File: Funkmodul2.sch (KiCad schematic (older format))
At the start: 48 parts, among them Q1 SSM3J334RLFTR-ND, Q2 AO3414, U1 MC74HC4538A, U2 MAX892, U3 ATMEGA128-16AU, Y1 Crystal_GND24

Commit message: Adds new unit
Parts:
- removed C1, C4: 10µF, Capacitors_SMD:C_1210_HandSoldering, symbol C
- removed C10, C11, C12, C20, C5, C6: 100nF, Capacitors_SMD:C_0603_HandSoldering, symbol C
- removed C2: 1µF, Capacitors_SMD:C_1210_HandSoldering, symbol C
- removed C3: 1nF, Capacitors_SMD:C_0603_HandSoldering, symbol C
- removed C7, C8: 10pF, Capacitors_SMD:C_0603_HandSoldering, symbol C
- removed C9: 10nF, Capacitors_SMD:C_0603_HandSoldering, symbol C
- removed D1, D2, D3, D4, D5, D6, D7, D8, D9: TS4148C, Diodes_SMD:D_0603, symbol D
- removed D10: DZ2J036M0LCT-ND, Diodes_SMD:D_SOD-323F, symbol D_Zener
- removed L1: 10nH, Inductors_SMD:L_0603_HandSoldering, symbol Ferrite_Bead
- removed Q1: SSM3J334RLFTR-ND, TO_SOT_Packages_SMD:SOT-23, symbol Q_PMOS_DGS
- removed Q2: AO3414, TO_SOT_Packages_SMD:SOT-23, symbol Q_NMOS_DGS
- removed R1: 22k, Resistors_SMD:R_0603_HandSoldering, symbol R
- removed R10: 15k, Resistors_SMD:R_0603_HandSoldering, symbol R
- removed R11, R14, R15, R16, R17, R2, R3, R6, R7, R9: 100k, Resistors_SMD:R_0603_HandSoldering, symbol R
- removed R12, R13, R8: 10k, Resistors_SMD:R_0603_HandSoldering, symbol R
- removed R18, R5: 100R, Resistors_SMD:R_0603_HandSoldering, symbol R
- removed R4: 47R, Resistors_SMD:R_0603_HandSoldering, symbol R
- removed U1: MC74HC4538A, Housings_SOIC:SOIC-16_3.9x9.9mm_Pitch1.27mm, symbol MC74HC4538A
- removed U2: MAX892, Maxim:µMAX-8, symbol MAX892
- removed U3: ATMEGA128-16AU, Housings_QFP:TQFP-64_14x14mm_Pitch0.8mm, symbol ATMEGA128-16AU
- removed Y1: Crystal_GND24, Crystals:Crystal_SMD_3225-4pin_3.2x2.5mm_HandSoldering, symbol Crystal_GND24
- added C21, C25: 10µF, Capacitors_SMD:C_1210_HandSoldering, symbol C
- added C22, C26, C27, C31, C32, C33: 100nF, Capacitors_SMD:C_0603_HandSoldering, symbol C
- added C23: 1µF, Capacitors_SMD:C_1210_HandSoldering, symbol C
- added C24: 1nF, Capacitors_SMD:C_0603_HandSoldering, symbol C
- added C28, C29: 10pF, Capacitors_SMD:C_0603_HandSoldering, symbol C
- added C30: 10nF, Capacitors_SMD:C_0603_HandSoldering, symbol C
- added D19, D20, D21, D22, D23, D24, D25, D26, D27: TS4148C, Diodes_SMD:D_0603, symbol D
- added D28: DZ2J036M0LCT-ND, Diodes_SMD:D_SOD-323F, symbol D_Zener
- added L3: 10nH, Inductors_SMD:L_0603_HandSoldering, symbol Ferrite_Bead
- added Q10: AO3414, TO_SOT_Packages_SMD:SOT-23, symbol Q_NMOS_DGS
- added Q9: SSM3J334RLFTR-ND, TO_SOT_Packages_SMD:SOT-23, symbol Q_PMOS_DGS
- added R46: 22k, Resistors_SMD:R_0603_HandSoldering, symbol R
- added R47, R48, R51, R52, R54, R56, R59, R60, R61, R62: 100k, Resistors_SMD:R_0603_HandSoldering, symbol R
- added R49: 47R, Resistors_SMD:R_0603_HandSoldering, symbol R
- added R50, R63: 100R, Resistors_SMD:R_0603_HandSoldering, symbol R
- added R53, R57, R58: 10k, Resistors_SMD:R_0603_HandSoldering, symbol R
- added R55: 15k, Resistors_SMD:R_0603_HandSoldering, symbol R
- added U6: MC74HC4538A, Housings_SOIC:SOIC-16_3.9x9.9mm_Pitch1.27mm, symbol MC74HC4538A
- added U7: MAX892, Maxim:µMAX-8, symbol MAX892
- added U8: ATMEGA128-16AU, Housings_QFP:TQFP-64_14x14mm_Pitch0.8mm, symbol ATMEGA128-16AU
- added Y2: Crystal_GND24, Crystals:Crystal_SMD_3225-4pin_3.2x2.5mm_HandSoldering, symbol Crystal_GND24

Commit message: Places µC of second module
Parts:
- Q9: symbol Q_PMOS_DGS -> Q_PMOS_SGD
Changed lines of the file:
@@
 $EndComp
 $Comp
-L GND #PWR57
+L GND #PWR047
 U 1 1 59B7E482
 P 3200 1650
-F 0 "#PWR57" H 3200 1400 50  0001 C CNN
+F 0 "#PWR047" H 3200 1400 50  0001 C CNN
 F 1 "GND" H 3200 1500 50  0000 C CNN
 F 2 "" H 3200 1650 50  0001 C CNN
@@
 $EndComp
 $Comp
-L GND #PWR53
+L GND #PWR048
 U 1 1 59FF9D56
 P 2250 1350
-F 0 "#PWR53" H 2250 1100 50  0001 C CNN
+F 0 "#PWR048" H 2250 1100 50  0001 C CNN
 F 1 "GND" H 2250 1200 50  0000 C CNN
 F 2 "" H 2250 1350 50  0001 C CNN
@@
 VCC
 $Comp
-L GND #PWR59
+L GND #PWR049
 U 1 1 59FF9D57
 P 3750 2450
-F 0 "#PWR59" H 3750 2200 50  0001 C CNN
+F 0 "#PWR049" H 3750 2200 50  0001 C CNN
 F 1 "GND" H 3750 2300 50  0000 C CNN
 F 2 "" H 3750 2450 50  0001 C CNN
@@
 $EndComp
 $Comp
-L GND #PWR60
+L GND #PWR050
 U 1 1 59FF9D58
 P 3750 2850
-F 0 "#PWR60" H 3750 2600 50  0001 C CNN
+F 0 "#PWR050" H 3750 2600 50  0001 C CNN
 F 1 "GND" H 3750 2700 50  0000 C CNN
 F 2 "" H 3750 2850 50  0001 C CNN
@@
 $EndComp
 $Comp
-L GND #PWR63
+L GND #PWR051
 U 1 1 59FF9D59
 P 4300 3350
-F 0 "#PWR63" H 4300 3100 50  0001 C CNN
+F 0 "#PWR051" H 4300 3100 50  0001 C CNN
 F 1 "GND" H 4300 3200 50  0000 C CNN
 F 2 "" H 4300 3350 50  0001 C CNN
@@
 $EndComp
 $Comp
-L GND #PWR64
+L GND #PWR052
 U 1 1 59B80EAC
 P 4550 2350
-F 0 "#PWR64" H 4550 2100 50  0001 C CNN
+F 0 "#PWR052" H 4550 2100 50  0001 C CNN
 F 1 "GND" H 4550 2200 50  0000 C CNN
 F 2 "" H 4550 2350 50  0001 C CNN
@@
 $EndComp
 $Comp
-L GND #PWR65
+L GND #PWR053
 U 1 1 59B80F3D
 P 5000 2350
-F 0 "#PWR65" H 5000 2100 50  0001 C CNN
+F 0 "#PWR053" H 5000 2100 50  0001 C CNN
 F 1 "GND" H 5000 2200 50  0000 C CNN
 F 2 "" H 5000 2350 50  0001 C CNN
@@
 $EndComp
 $Comp
-L GND #PWR70
+L GND #PWR054
 U 1 1 59B835F0
 P 7000 1100
-F 0 "#PWR70" H 7000 850 50  0001 C CNN
+F 0 "#PWR054" H 7000 850 50  0001 C CNN
 F 1 "GND" H 7000 950 50  0000 C CNN
 F 2 "" H 7000 1100 50  0001 C CNN
@@
 $EndComp
 $Comp
-L GND #PWR67
+L GND #PWR055
 U 1 1 59B83656
 P 6500 1150
-F 0 "#PWR67" H 6500 900 50  0001 C CNN
+F 0 "#PWR055" H 6500 900 50  0001 C CNN
 F 1 "GND" H 6500 1000 50  0000 C CNN
 F 2 "" H 6500 1150 50  0001 C CNN
@@
 $EndComp
 $Comp
-L GND #PWR66
+L GND #PWR056
 U 1 1 59B836BC
 P 6200 1150
-F 0 "#PWR66" H 6200 900 50  0001 C CNN
+F 0 "#PWR056" H 6200 900 50  0001 C CNN
 F 1 "GND" H 6200 1000 50  0000 C CNN
 F 2 "" H 6200 1150 50  0001 C CNN
@@
 $EndComp
 $Comp
-L GND #PWR68
+L GND #PWR057
 U 1 1 59FF9D5F
 P 6600 5700
-F 0 "#PWR68" H 6600 5450 50  0001 C CNN
+F 0 "#PWR057" H 6600 5450 50  0001 C CNN
 F 1 "GND" H 6600 5550 50  0000 C CNN
 F 2 "" H 6600 5700 50  0001 C CNN
@@
 $EndComp
 $Comp
-L GND #PWR69
+L GND #PWR058
 U 1 1 59FF9D60
 P 6700 5700
-F 0 "#PWR69" H 6700 5450 50  0001 C CNN
+F 0 "#PWR058" H 6700 5450 50  0001 C CNN
 F 1 "GND" H 6700 5550 50  0000 C CNN
 F 2 "" H 6700 5700 50  0001 C CNN
@@
 $EndComp
 $Comp
-L GND #PWR71
+L GND #PWR059
 U 1 1 59FF9D61
 P 7000 5700
-F 0 "#PWR71" H 7000 5450 50  0001 C CNN
+F 0 "#PWR059" H 7000 5450 50  0001 C CNN
 F 1 "GND" H 7000 5550 50  0000 C CNN
 F 2 "" H 7000 5700 50  0001 C CNN
@@
 $EndComp
 $Comp
-L GND #PWR51
+L GND #PWR060
 U 1 1 59FF9D65
 P 1650 2750
-F 0 "#PWR51" H 1650 2500 50  0001 C CNN
+F 0 "#PWR060" H 1650 2500 50  0001 C CNN
 F 1 "GND" H 1650 2600 50  0000 C CNN
 F 2 "" H 1650 2750 50  0001 C CNN
@@
 $EndComp
 $Comp
-L GND #PWR58
+L GND #PWR061
 U 1 1 59FF9D69
 P 3600 750
-F 0 "#PWR58" H 3600 500 50  0001 C CNN
+F 0 "#PWR061" H 3600 500 50  0001 C CNN
 F 1 "GND" H 3600 600 50  0000 C CNN
 F 2 "" H 3600 750 50  0001 C CNN
@@
 $EndComp
 $Comp
-L GND #PWR52
+L GND #PWR062
 U 1 1 59B8D515
 P 1750 750
-F 0 "#PWR52" H 1750 500 50  0001 C CNN
+F 0 "#PWR062" H 1750 500 50  0001 C CNN
 F 1 "GND" H 1750 600 50  0000 C CNN
 F 2 "" H 1750 750 50  0001 C CNN
@@
 $EndComp
 $Comp
-L GND #PWR54
+L GND #PWR063
 U 1 1 59B94F70
 P 2650 4050
-F 0 "#PWR54" H 2650 3800 50  0001 C CNN
+F 0 "#PWR063" H 2650 3800 50  0001 C CNN
 F 1 "GND" H 2650 3900 50  0000 C CNN
 F 2 "" H 2650 4050 50  0001 C CNN
@@
 $EndComp
 $Comp
-L GND #PWR47
+L GND #PWR064
 U 1 1 59C3023F
 P 600 1500
-F 0 "#PWR47" H 600 1250 50  0001 C CNN
+F 0 "#PWR064" H 600 1250 50  0001 C CNN
 F 1 "GND" H 600 1350 50  0000 C CNN
 F 2 "" H 600 1500 50  0001 C CNN
@@
 $EndComp
 $Comp
-L GND #PWR48
+L GND #PWR065
 U 1 1 59FF9D7D
 P 800 4850
-F 0 "#PWR48" H 800 4600 50  0001 C CNN
+F 0 "#PWR065" H 800 4600 50  0001 C CNN
 F 1 "GND" H 800 4700 50  0000 C CNN
 F 2 "" H 800 4850 50  0001 C CNN
@@
 $EndComp
 $Comp
-L GND #PWR56
+L GND #PWR066
 U 1 1 59FF9D81
 P 2950 3100
-F 0 "#PWR56" H 2950 2850 50  0001 C CNN
+F 0 "#PWR066" H 2950 2850 50  0001 C CNN
 F 1 "GND" H 2950 2950 50  0000 C CNN
 F 2 "" H 2950 3100 50  0001 C CNN
@@
 $EndComp
 $Comp
-L GND #PWR49
+L GND #PWR067
 U 1 1 59FF9D84
 P 1350 3400
-F 0 "#PWR49" H 1350 3150 50  0001 C CNN
+F 0 "#PWR067" H 1350 3150 50  0001 C CNN
 F 1 "GND" H 1350 3250 50  0000 C CNN
 F 2 "" H 1350 3400 50  0001 C CNN
@@
 $EndComp
 $Comp
-L GND #PWR55
+L GND #PWR068
 U 1 1 59FF9D8A
 P 2700 5750
-F 0 "#PWR55" H 2700 5500 50  0001 C CNN
+F 0 "#PWR068" H 2700 5500 50  0001 C CNN
 F 1 "GND" H 2700 5600 50  0000 C CNN
 F 2 "" H 2700 5750 50  0001 C CNN
@@
 $EndComp
 $Comp
-L GND #PWR61
+L GND #PWR069
 U 1 1 59FF9D8E
 P 3750 5550
-F 0 "#PWR61" H 3750 5300 50  0001 C CNN
+F 0 "#PWR069" H 3750 5300 50  0001 C CNN
 F 1 "GND" H 3750 5400 50  0000 C CNN
 F 2 "" H 3750 5550 50  0001 C CNN
@@
 $EndComp
 $Comp
-L GND #PWR62
+L GND #PWR070
 U 1 1 59FF9D91
 P 3950 5500
-F 0 "#PWR62" H 3950 5250 50  0001 C CNN
+F 0 "#PWR070" H 3950 5250 50  0001 C CNN
 F 1 "GND" H 3950 5350 50  0000 C CNN
 F 2 "" H 3950 5500 50  0001 C CNN
@@
 VCC
 $Comp
-L GND #PWR72
+L GND #PWR071
 U 1 1 59FF9DA5
 P 9100 1450
-F 0 "#PWR72" H 9100 1200 50  0001 C CNN
+F 0 "#PWR071" H 9100 1200 50  0001 C CNN
 F 1 "GND" H 9100 1300 50  0000 C CNN
 F 2 "" H 9100 1450 50  0001 C CNN
@@
 $EndComp
 $Comp
-L GND #PWR50
+L GND #PWR072
 U 1 1 59DB2AE7
 P 1600 2400
-F 0 "#PWR50" H 1600 2150 50  0001 C CNN
+F 0 "#PWR072" H 1600 2150 50  0001 C CNN
 F 1 "GND" H 1600 2250 50  0000 C CNN
 F 2 "" H 1600 2400 50  0001 C CNN
@@
 3.3V
 $Comp
-L Q_PMOS_DGS Q9
+L Q_PMOS_SGD Q9
 U 1 1 59F0FE2A
 P 1400 1500

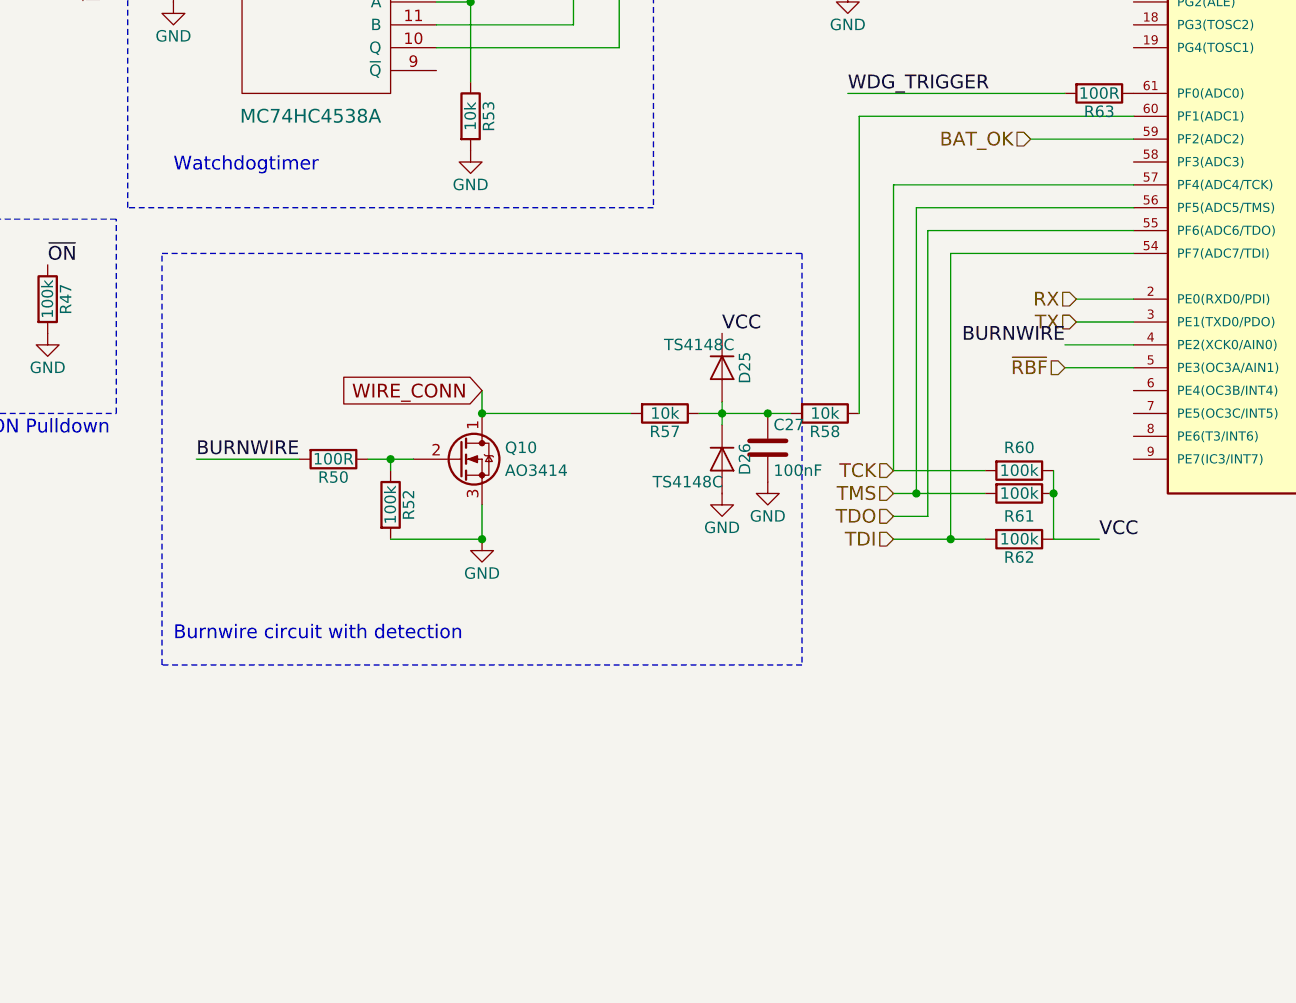
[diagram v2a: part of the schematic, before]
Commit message: Places all Components of second module
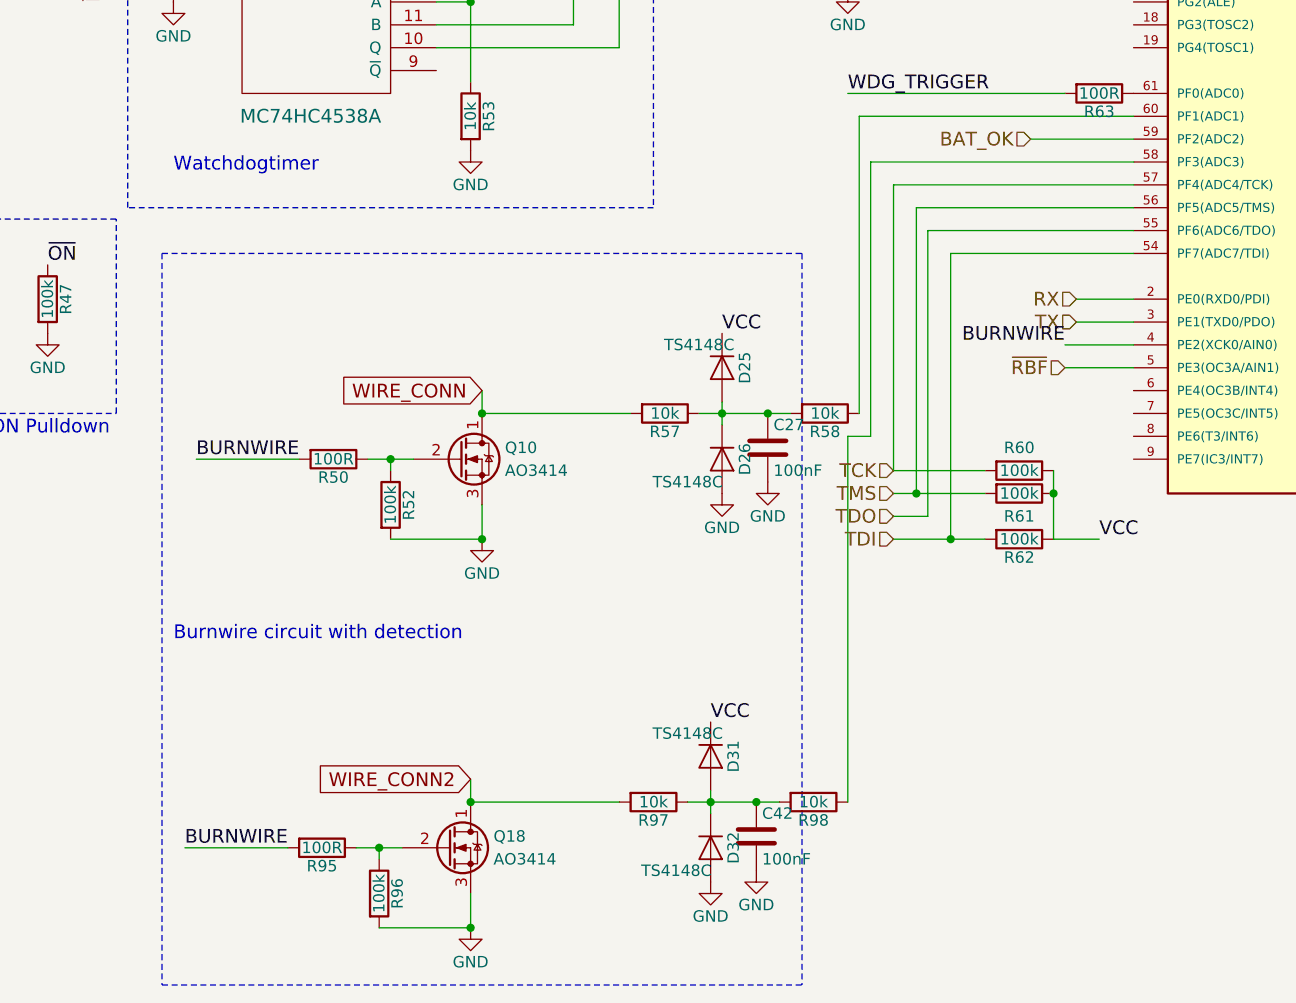
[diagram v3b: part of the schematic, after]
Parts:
- added C42: 100nF, Capacitors_SMD:C_0603_HandSoldering, symbol C
- added D31, D32: TS4148C, Diodes_SMD:D_0603, symbol D
- added Q18: AO3414, TO_SOT_Packages_SMD:SOT-23, symbol Q_NMOS_DGS
- added R95: 100R, Resistors_SMD:R_0603_HandSoldering, symbol R
- added R96: 100k, Resistors_SMD:R_0603_HandSoldering, symbol R
- added R97, R98: 10k, Resistors_SMD:R_0603_HandSoldering, symbol R
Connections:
- net BURNWIRE: now also R95.2
- net GND: now also C42.2, D32.2 (A), Q18.3 (S), R96.2
- net VCC: now also D31.1 (K)
- net at U8.58 (PF3(ADC3)): now also R98.1
- new net: Q18.2 (G), R95.1, R96.1
- new net: C42.1, D31.2 (A), D32.1 (K), R97.1, R98.2
- new net WIRE_CONN2: Q18.1 (D), R97.2
